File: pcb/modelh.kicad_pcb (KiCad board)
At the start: 2 copper layers, 150 x 38 mm, 67 parts, among them SW1 SW_Push, U1 GD32F103C8T6, U2 AMS1117-3.3, Y1 8MHz

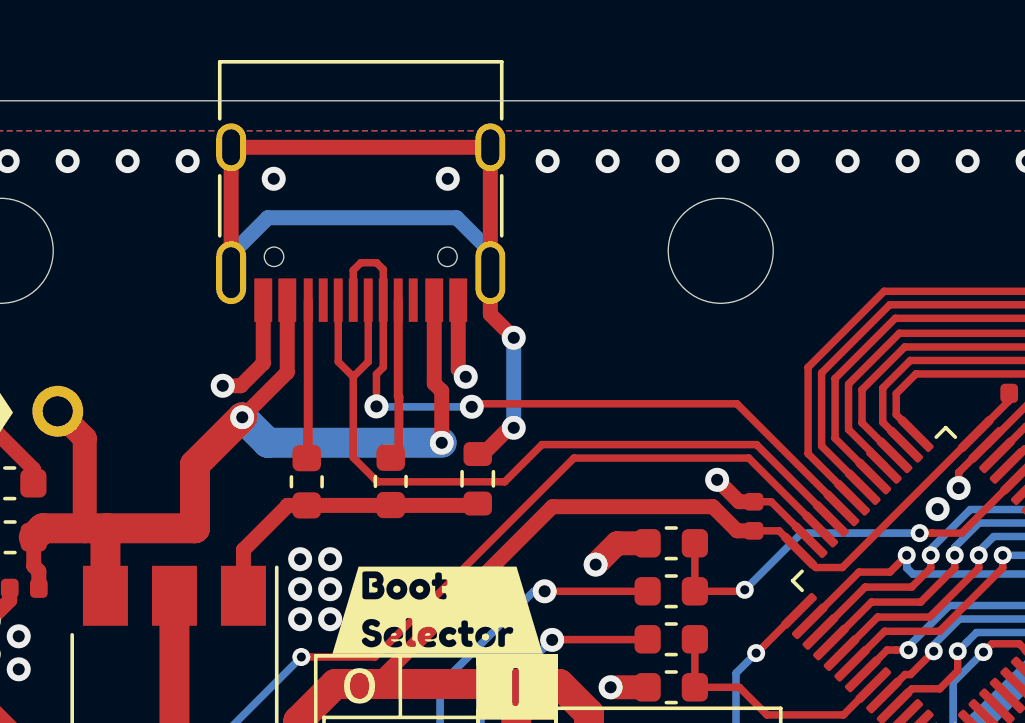
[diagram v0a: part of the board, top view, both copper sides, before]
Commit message: Places USB C connector completely inside the board
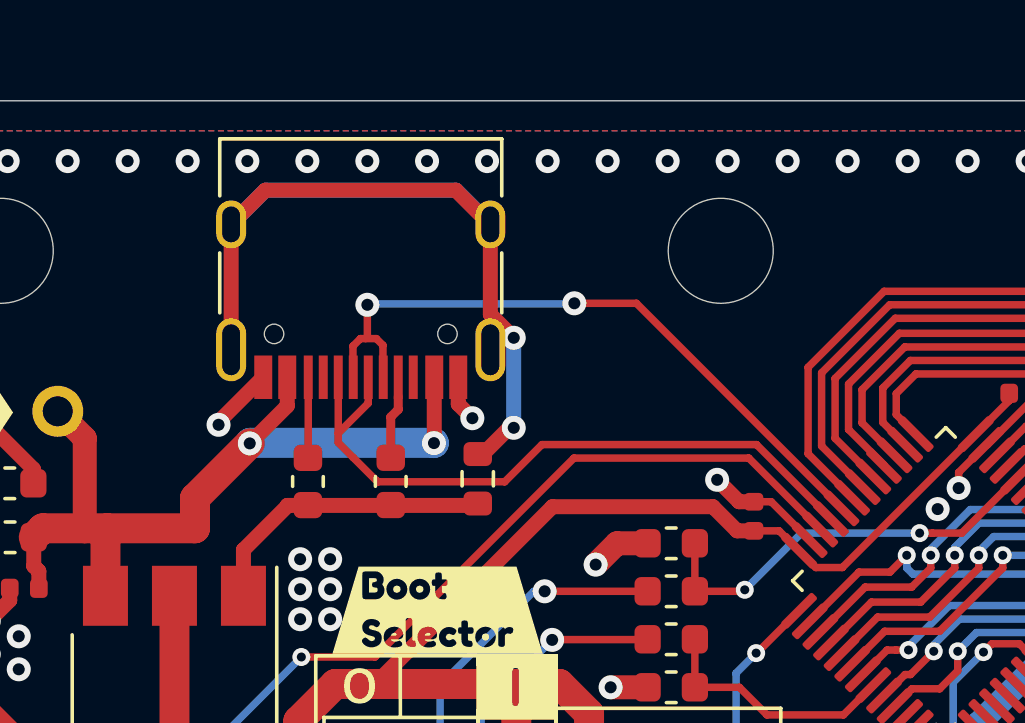
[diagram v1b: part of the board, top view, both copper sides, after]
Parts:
- moved USB_C1 2.57 mm to (88.8, 52.2)
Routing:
- net +5V: track 34.8 -> 28.6 mm
- net Net-(R3-Pad1): track 5.38 -> 2.15 mm
- net D+: track 26.0 -> 22.9 mm
- net Net-(R11-Pad2): track 35.0 -> 32.0 mm
- net GND: track 58.8 -> 56.2 mm, vias 262 -> 265
- net Net-(R4-Pad1): track 5.22 -> 2.65 mm

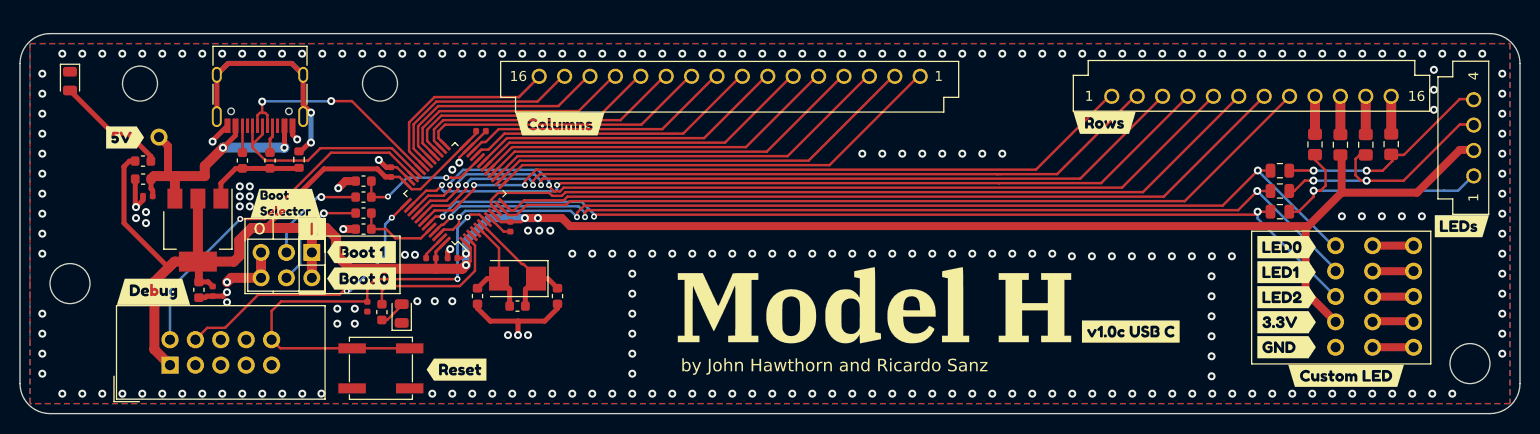
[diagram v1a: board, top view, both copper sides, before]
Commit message: Adds missing 1.5k pullup resistor to USB D+ line
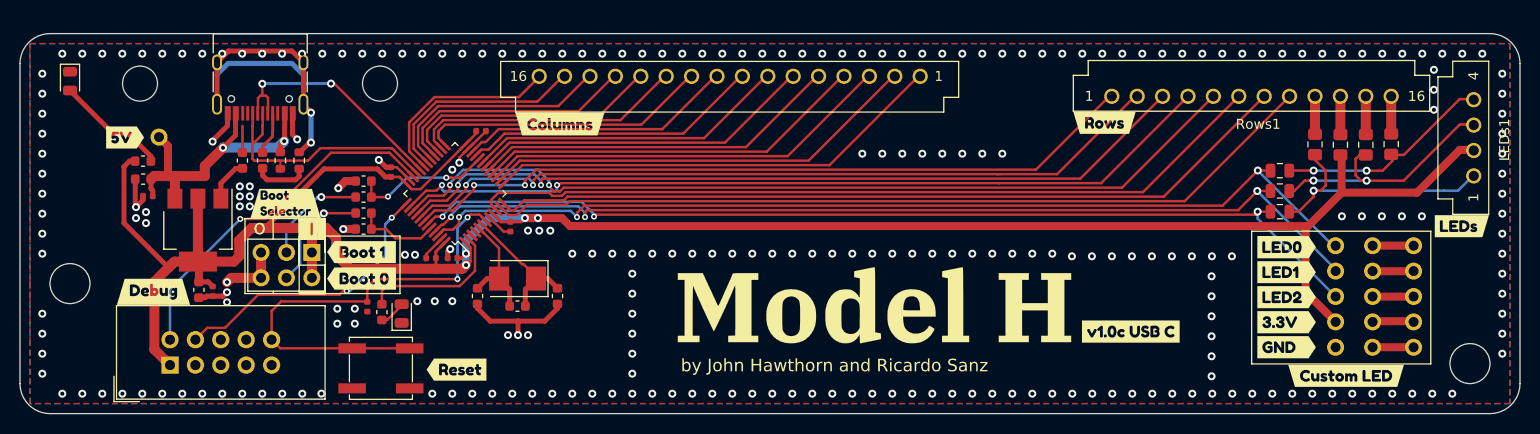
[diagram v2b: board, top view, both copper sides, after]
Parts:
- added R16: 1.5k, Resistor_SMD:R_0603_1608Metric, F.Cu at (90.8, 59.7)
- moved USB_C1 1.24 mm to (88.8, 50.9)
- moved R3 0.74 mm to (89.0, 59.7)
- moved R11 0.09 mm to (92.7, 59.7)
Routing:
- net D+: track 22.9 -> 26.9 mm
- net +5V: track 28.6 -> 32.1 mm
- net GND: track 56.2 -> 58.5 mm, vias 265 -> 262
- net Net-(R3-Pad1): track 2.15 -> 4.35 mm
- net D-: track 22.9 -> 23.6 mm
- net Net-(R11-Pad2): vias 2 -> 5

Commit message: Update schematics and pcb
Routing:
- net +3V3: track 234.8 -> 238.7 mm
- net GND: track 58.5 -> 55.9 mm
- net +5V: track 32.1 -> 29.7 mm
- net Net-(R3-Pad1): track 4.35 -> 2.40 mm
- net D+: track 26.9 -> 25.2 mm
- net OSC8OUT: track 11.6 -> 12.6 mm
- net SWDIO: track 36.0 -> 35.1 mm
- net SWCLK: track 28.6 -> 27.8 mm
- net row4: track 87.2 -> 86.5 mm
- net col1: track 21.6 -> 20.9 mm
- net row1: track 78.2 -> 77.6 mm
- net row2: track 81.3 -> 80.6 mm
- net col2: track 23.2 -> 22.5 mm
- net nRST: track 46.7 -> 46.1 mm
- net row0: track 74.6 -> 74.0 mm
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
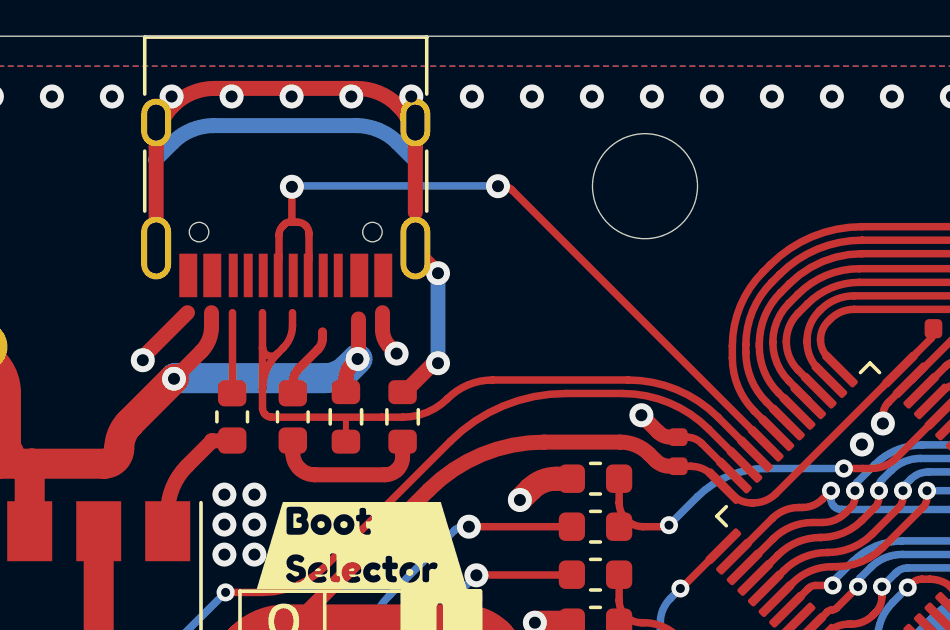
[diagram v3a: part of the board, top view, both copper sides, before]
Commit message: Add proper CC resistors for USB C
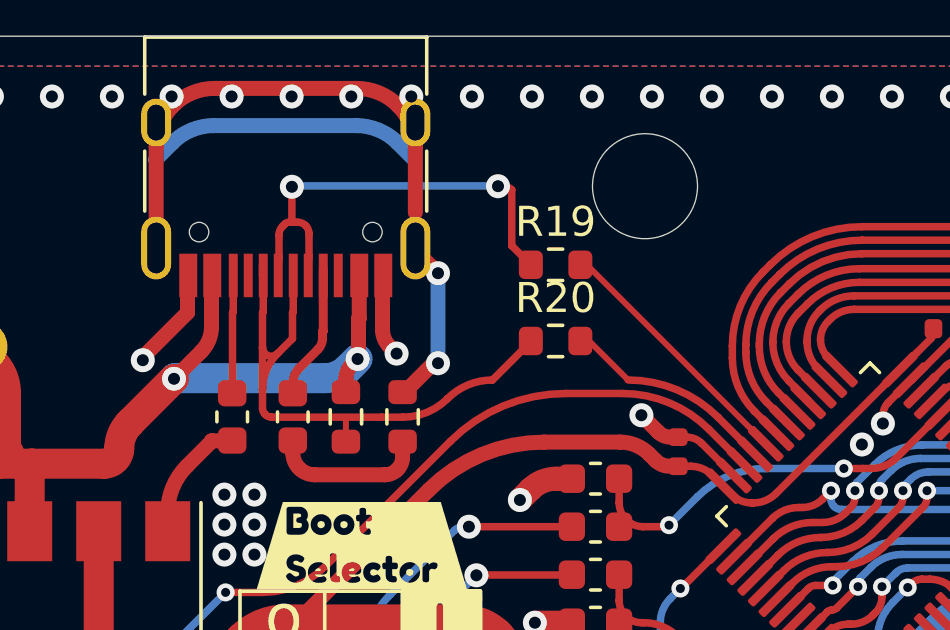
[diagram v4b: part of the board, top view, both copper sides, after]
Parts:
- added R19: 22, Resistor_SMD:R_0603_1608Metric, F.Cu at (97.8, 54.6)
- added R20: 22, Resistor_SMD:R_0603_1608Metric, F.Cu at (97.8, 57.1)
- R3, R4: value 22 -> 5.1k
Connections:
- R16 pad 1: D+ -> Net-(USB_C1-PadA6)
- USB_C1 pad A6: D+ -> Net-(USB_C1-PadA6)
- USB_C1 pad A7: D- -> Net-(USB_C1-PadA7)
- USB_C1 pad B6: D+ -> Net-(USB_C1-PadA6)
- USB_C1 pad B7: D- -> Net-(USB_C1-PadA7)
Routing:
- net Net-(USB_C1-PadA6): track 0.00 -> 20.3 mm
- net D+: track 25.2 -> 7.19 mm
- net D-: track 23.5 -> 8.65 mm, vias 2 -> 0
- net Net-(USB_C1-PadA7): track 0.00 -> 14.3 mm, vias 0 -> 2
- net +5V: track 29.7 -> 32.4 mm
- net GND: track 55.9 -> 58.4 mm
- net Net-(R3-Pad1): track 2.40 -> 4.52 mm
- net Net-(R4-Pad1): track 2.65 -> 3.90 mm
